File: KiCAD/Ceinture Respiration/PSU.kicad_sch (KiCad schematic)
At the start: 8 parts, among them J11 Conn_01x02, Q2 AP10N04S

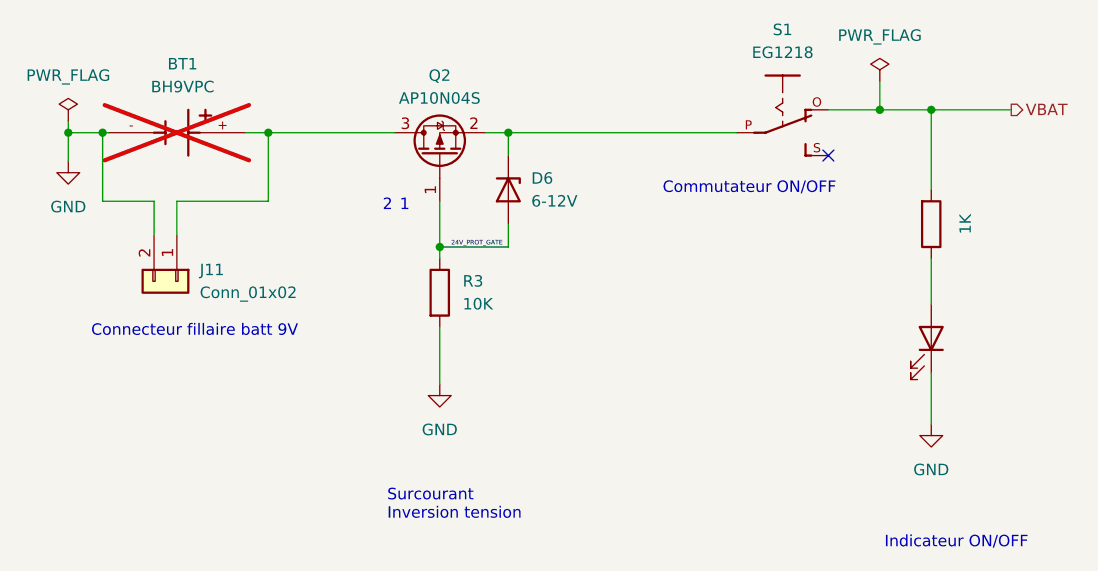
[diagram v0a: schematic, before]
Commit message: sch 99% pcb 85%
Ajout de l'ensemble des traces du pcb mère
Ajout de via stiching
Reste le PCB shield à terminer
Reste les erreurs générés à nettoyer
Brûlé le gars...
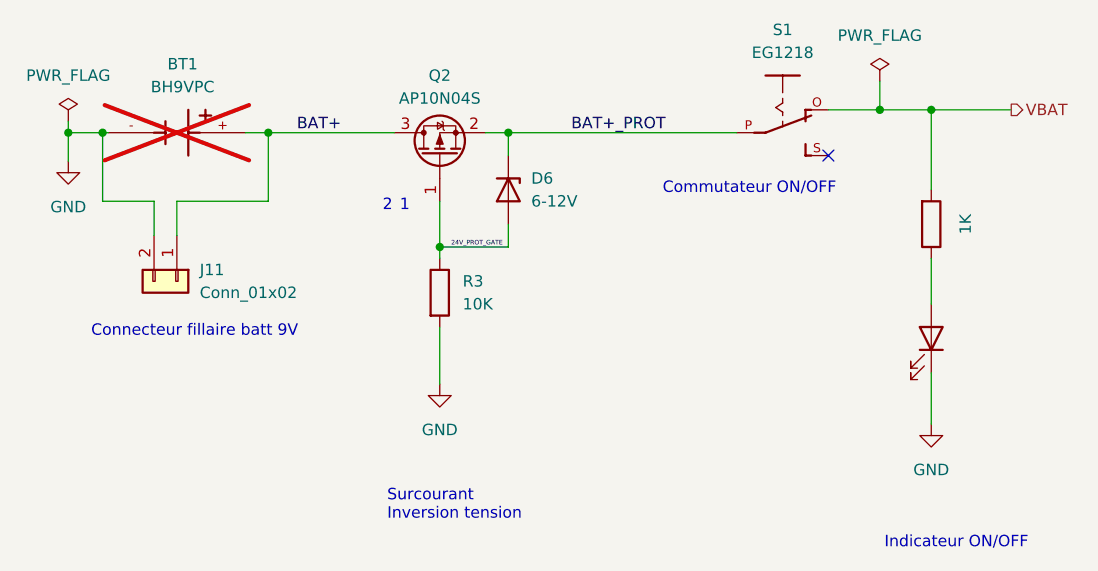
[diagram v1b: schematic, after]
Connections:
- net BAT+: now reaches BT1.+, J11.1 (Pin_1), Q2.3 (D)
- net BAT+_PROT: now reaches D6.1 (K), Q2.2 (S), S1.P
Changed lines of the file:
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@@
+    (effects (font (size 1.27 1.27)) (justify left bottom))
+  )
+  (label "BAT+_PROT" (at 111.125 47.625 0) (fields_autoplaced)
+    (effects (font (size 1.27 1.27)) (justify left bottom))
+  )
+  (label "BAT+" (at 80.645 47.625 0) (fields_autoplaced)
     (effects (font (size 1.27 1.27)) (justify left bottom))
   )

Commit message: PCB sent for production
See latest production files.
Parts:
- R3: footprint Resistor_SMD:R_0402_1005Metric -> Resistor_SMD:R_0603_1608Metric; LCSC C25744 -> C25804
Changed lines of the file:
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@@
       (effects (font (size 1.27 1.27)) (justify left))
     )
-    (property "Footprint" "Resistor_SMD:R_0402_1005Metric" (at 94.742 65.405 90)
+    (property "Footprint" "Resistor_SMD:R_0603_1608Metric" (at 94.742 65.405 90)
       (effects (font (size 1.27 1.27)) hide)
     )
@@
       (effects (font (size 1.27 1.27)) hide)
     )
-    (property "LCSC" "C25744" (at 96.52 65.405 0)
+    (property "LCSC" "C25804" (at 96.52 65.405 0)
       (effects (font (size 1.27 1.27)) hide)
     )
